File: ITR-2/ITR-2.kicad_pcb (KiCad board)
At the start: 2 copper layers, 45 parts, among them X3 ico*отверстие*D1.2, X4 ico*отверстие*D1.2, X6 ico*отверстие*D1.2, X7 ico*отверстие*D1.2

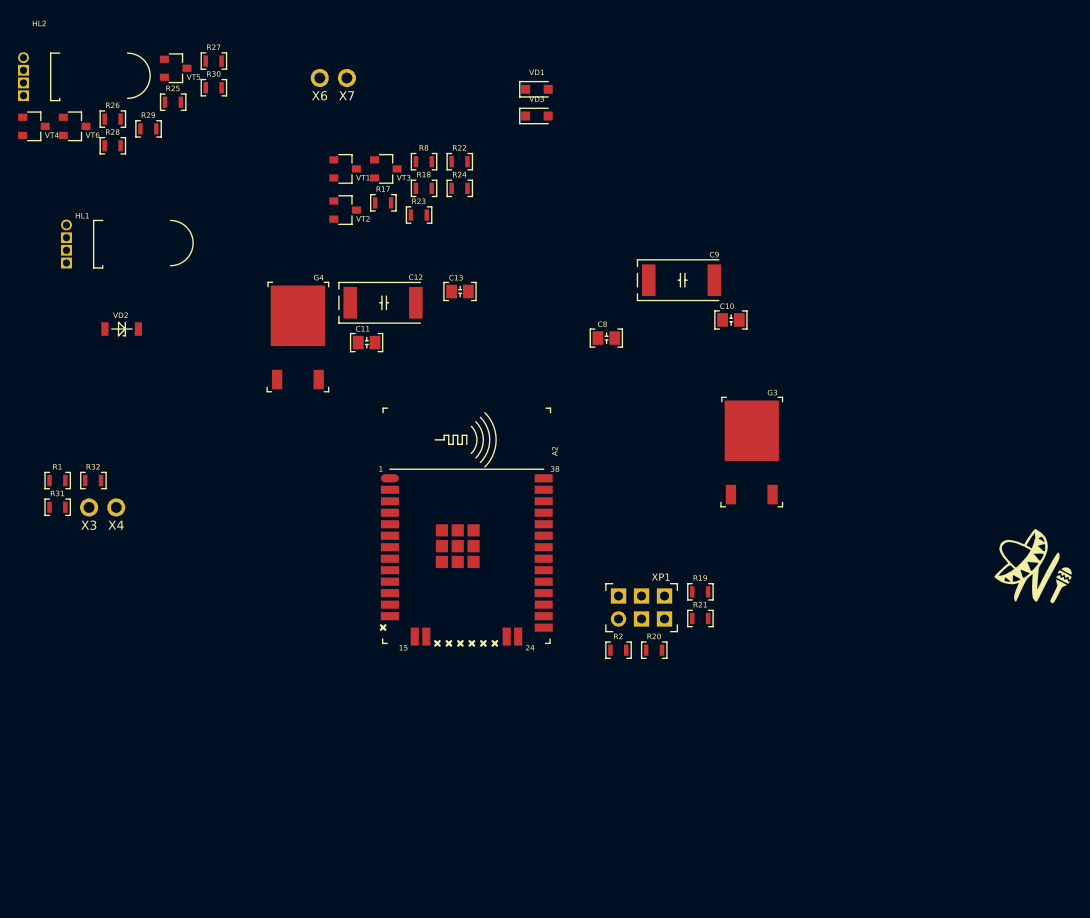
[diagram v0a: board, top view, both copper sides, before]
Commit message: проект платы 20х14,5
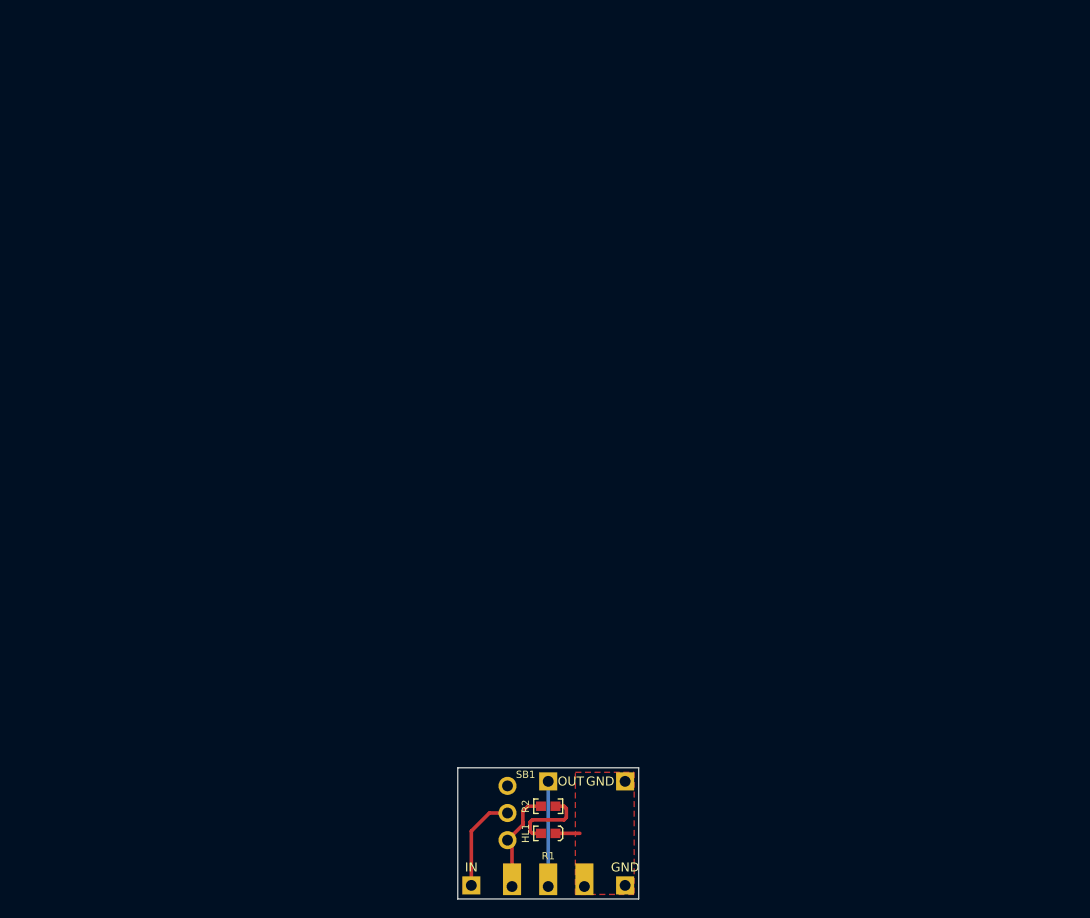
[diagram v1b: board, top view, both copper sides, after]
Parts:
- removed A2: МК*esp32_wroom_32*SMD_noSD, N_A:ESP32_WROOM32_pnp_noSD
- removed C10, C11, C13, C8: smd-конденсатор-керамика*0,1мк*25В*0805*импорт, MOTOR_RLC:Конденсатор_SMD_IEC_0805
- removed C12, C9: smd-конденсатор-тантал*22мк*32В*E*импорт, MOTOR_RLC:Конденсатор_тантал_SMD_m7343
- removed D1: LOGO, N_ICO:ni_10x10
- removed G3: Микросхема*LDO*IN30V*OUT3V3*0.15A*КТ-89*ОТК, MOTOR_VD_VT_HL:Корпус_КТ-89
- removed G4: Микросхема*LDO*IN30V*OUT5V*0.15A*КТ-89*ОТК, MOTOR_VD_VT_HL:Корпус_КТ-89
- removed HL2: Светодиод*RGB-CA*выводной-5мм*угловой, N_VD_HL:LED-RGB-5mm-выводной, угловой
- removed R17, R18, R25, R26, R27, R8: Резистор*1кОм*0603, N_RLC:Резистор_SMD_0603_0,065_Вт_pnp
- removed R19, R31, R32: Резистор*10кОм*0603, N_RLC:Резистор_SMD_0603_0,065_Вт_pnp
- removed R20, R21: Резистор*240_Ом*0603, N_RLC:Резистор_SMD_0603_0,065_Вт_pnp
- removed R22, R23, R24, R28, R29, R30: Резистор*49,9Ом*0603, N_RLC:Резистор_SMD_0603_0,065_Вт_pnp
- removed VD1, VD3: Диод*75В*0,2А*SOD-323, N_VD_HL:D_SOD-323_HandSoldering
- removed VD2: Стабилитрон*3,9В*SOD80, N_VD_HL:SOD-80
- removed VT1, VT2, VT3, VT4, VT5, VT6: Транзистор*npn*0,5А*45В*SOT23, N_VD_HL:Корпус_КТ-46
- removed X6, X7: ico*отверстие*D1.2, N_X:ОтверстиеD1.2
- removed XP1: Вилка*PLD*6контактов*2ряда*вертикальная, N_X:Вилка_PLD6_вертикальная_AB
- added SB1: DIP-переключатель_KLS7-SS-12F19-G5, Library:KLS7-SS-12F19-G5, F.Cu at (105.5, 108.0)
- added X1: ico*группа_монтажных_отв.&1шт_1.2мм, MOTOR_ICO:Отверстие_под_пайку_D1.2, F.Cu at (101.5, 113.0)
- added X2: ico*группа_монтажных_отв.&1шт_1.2мм, MOTOR_ICO:Отверстие_под_пайку_D1.2, F.Cu at (118.5, 113.0)
- HL1: value Светодиод*RGB-CA*выводной-5мм*угловой -> smd-светодиод*зеленый*10мА*0603*ВП; footprint N_VD_HL:LED-RGB-5mm-выводной, угловой -> MOTOR_VD_VT_HL:Светодиод_SMD_IEC_0603(AK)
- R1: value Резистор*10кОм*0603 -> DIP-переменный_резистор_R1001N12B1-A10K_вертикальный; footprint N_RLC:Резистор_SMD_0603_0,065_Вт_pnp -> Library:R1001N12B1-A10K-vertical
- R2: value Резистор*10кОм*0603 -> smd-резистор*4,7к*0603*ВП; footprint N_RLC:Резистор_SMD_0603_0,065_Вт_pnp -> MOTOR_RLC:Резистор_SMD_IEC_0603-0,075_Вт
- X3, X4: value ico*отверстие*D1.2 -> ico*группа_монтажных_отв.&1шт_1.2мм; footprint N_X:ОтверстиеD1.2 -> MOTOR_ICO:Отверстие_под_пайку_D1.2
- moved HL1 85.8 mm to (110.0, 107.2)
- moved R1 67.4 mm to (106.0, 113.1)
- moved X4 63.9 mm to (118.5, 101.5)
- moved X3 59.1 mm to (110.0, 101.5)
- moved R2 18.9 mm to (110.0, 104.2)
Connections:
- net 3V3 renamed Net-(R2-Pad1)
- R1 pad 2: /ADC-REF -> Net-(X3-Pad1)
- R2 pad 2: /RESET -> Net-(R2-Pad2)
- X3 pad 1: /ADC-NTC -> Net-(X3-Pad1)
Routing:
- net Net-(X3-Pad1): track 0.00 -> 11.6 mm
- net Net-(R2-Pad1): track 0.00 -> 11.5 mm
- net /9V-IN: track 0.00 -> 10.8 mm
- net Net-(R2-Pad2): track 0.00 -> 8.81 mm
- net GND: track 0.00 -> 2.70 mm
- added copper zone on F.Cu, net GND
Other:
- board outline added: 20 x 14.5 mm
- net class Default removed
- rule pad_to_mask_clearance: 0.051 -> 0
- board text added: "GND"
- board text added: "IN"
- board text added: "OUT"

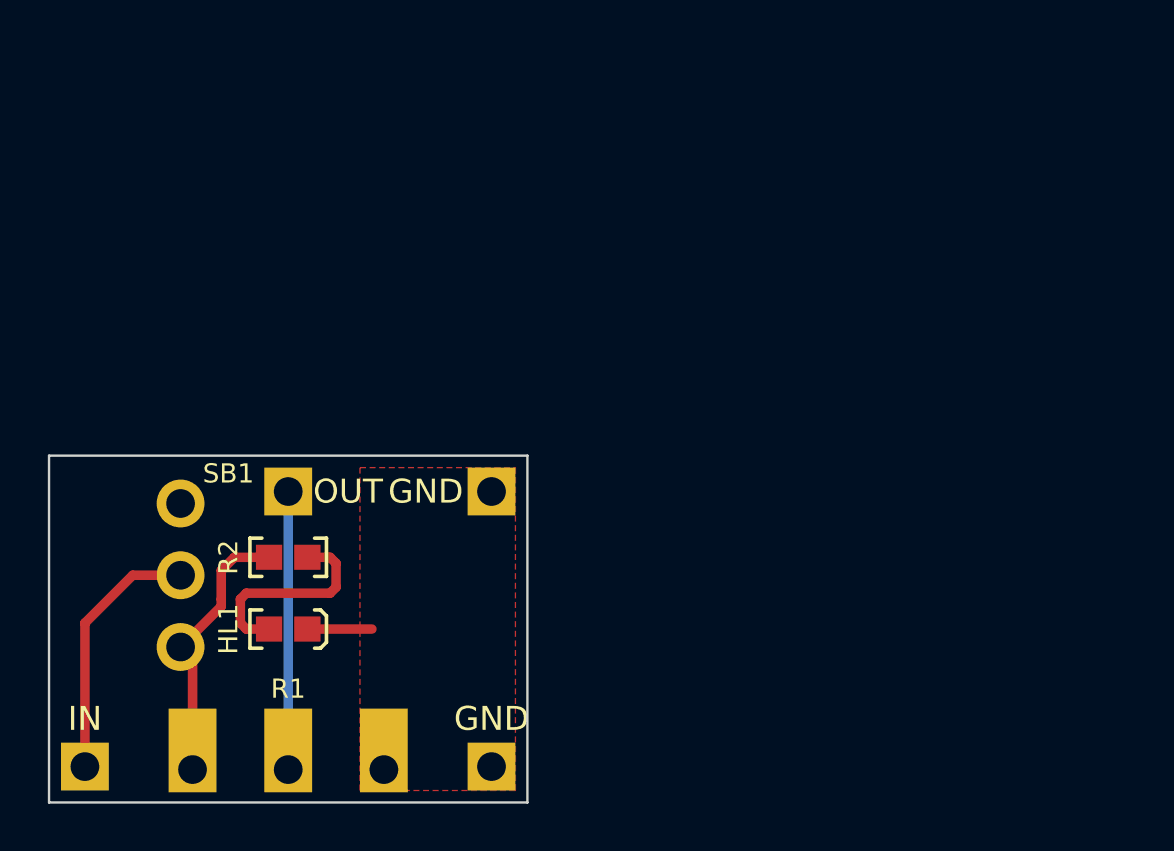
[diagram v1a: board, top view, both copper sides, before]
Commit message: Т-образная плата с повторителем и контроле напряжения на ОУ
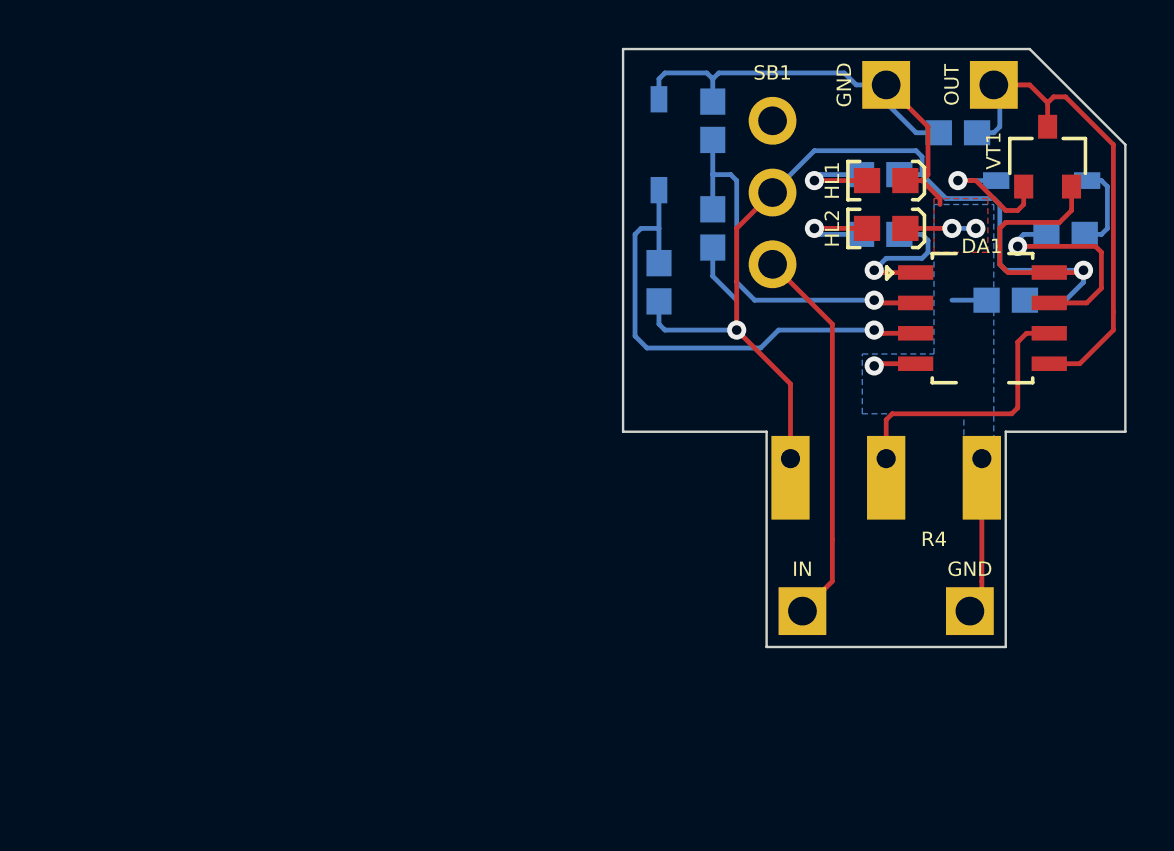
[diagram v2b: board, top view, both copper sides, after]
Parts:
- added C1: smd-конденсатор-керамика*0,01мк*25В*0603*ВП, MOTOR_RLC:Конденсатор_SMD_IEC_0603, B.Cu at (140.0, 93.5)
- added C2: smd-конденсатор-керамика*0,01мк*25В*0603*ВП, MOTOR_RLC:Конденсатор_SMD_IEC_0603, B.Cu at (138.0, 86.5)
- added DA1: ОУ*сдвоенный*so-8*ОТК, MOTOR_IMPORT_OTK:SO-8, F.Cu at (136.3, 92.4)
- added HL2: smd-светодиод*красный*10мА*0603*ВП, MOTOR_VD_VT_HL:Светодиод_SMD_IEC_0603(AK), F.Cu at (135.0, 90.5)
- added R2: smd-резистор*4,7к*0603*ВП, KICAD6_RLC:Резистор_SMD_IEC_0603-0,1_Вт, B.Cu at (134.8, 90.8)
- added R3: smd-резистор*10к*0,1Вт*5проц*0603*ВП, KICAD6_RLC:Резистор_SMD_IEC_0603-0,1_Вт, B.Cu at (125.5, 92.8)
- added R5: smd-резистор*10к*0,1Вт*5проц*0603*ВП, KICAD6_RLC:Резистор_SMD_IEC_0603-0,1_Вт, B.Cu at (127.8, 90.5)
- added R6: smd-резистор*10к*0,1Вт*5проц*0603*ВП, KICAD6_RLC:Резистор_SMD_IEC_0603-0,1_Вт, B.Cu at (127.8, 86.0)
- added R7: smd-резистор*4,7к*0603*ВП, KICAD6_RLC:Резистор_SMD_IEC_0603-0,1_Вт, B.Cu at (142.5, 90.8)
- added VD1: smd-стабилитрон*6,8В*5мА*КД-36*ОТК, MOTOR_VD_VT_HL:Корпус_IEC_КД-36, B.Cu at (125.5, 87.0)
- added VD2: smd-стабилитрон*6,8В*5мА*КД-36*ОТК, MOTOR_VD_VT_HL:Корпус_IEC_КД-36, B.Cu at (141.5, 88.5)
- added VT1: smd-транзистор*pnp*0,5А*50В*КТ-46*ОТК, MOTOR_VD_VT_HL:Корпус_КТ-46, F.Cu at (141.8, 87.5)
- R1: renamed from R2; footprint MOTOR_RLC:Резистор_SMD_IEC_0603-0,075_Вт -> KICAD6_RLC:Резистор_SMD_IEC_0603-0,1_Вт; moved to B.Cu
- moved R4 35.5 mm to (139.0, 100.1), turned to 180 degrees
- moved X3 34.0 mm to (139.5, 84.5)
- moved HL1 31.2 mm to (135.0, 88.5)
- moved X1 30.7 mm to (131.5, 106.5)
- moved R1 29.5 mm to (134.8, 88.2), turned to 180 degrees
- moved SB1 29.5 mm to (130.2, 92.0)
- moved X4 23.7 mm to (135.0, 84.5)
- moved X2 21.0 mm to (138.5, 106.5)
- renumbered R1 to R4
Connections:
- R1 pad 1: Net-(R2-Pad1) -> 9V
- R4 pad 1: Net-(R2-Pad1) -> GND
- R4 pad 2: Net-(X3-Pad1) -> AREF
- R4 pad 3: GND -> 9V
- SB1 pad 1: Net-(R2-Pad1) -> /9V-IN
- SB1 pad 2: /9V-IN -> 9V
- X3 pad 1: Net-(X3-Pad1) -> /UOUT
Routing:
- net 9V: track 0.00 -> 52.1 mm, vias 0 -> 2
- net GND: track 2.70 -> 34.6 mm, vias 0 -> 3
- net /UOUT: track 0.00 -> 21.2 mm
- net 2V5: track 0.00 -> 20.7 mm, vias 0 -> 1
- net /SENS: track 0.00 -> 16.1 mm, vias 0 -> 1
- net Net-(X3-Pad1): track 11.6 -> 0.00 mm
- net AREF: track 0.00 -> 11.6 mm
- net Net-(R2-Pad1): track 11.5 -> 0.00 mm
- net /DIRECT: track 0.00 -> 9.09 mm, vias 0 -> 1
- net /ALARM-LED: track 0.00 -> 6.14 mm, vias 0 -> 1
- net Net-(VD2-PadK): track 0.00 -> 5.72 mm, vias 0 -> 1
- net /9V-IN: track 10.8 -> 16.1 mm
- net Net-(HL1-PadA): track 8.81 -> 4.25 mm, vias 0 -> 1
- net Net-(HL2-PadA): track 0.00 -> 4.25 mm, vias 0 -> 1
- net Net-(R7-Pad1): track 0.00 -> 3.76 mm
- added copper zone on B.Cu, net GND
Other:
- board size 20 x 14.5 mm -> 21 x 25 mm
